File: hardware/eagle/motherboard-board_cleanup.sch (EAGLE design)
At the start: 43 parts, among them U1 DG412DJZ, Y1 16MHz

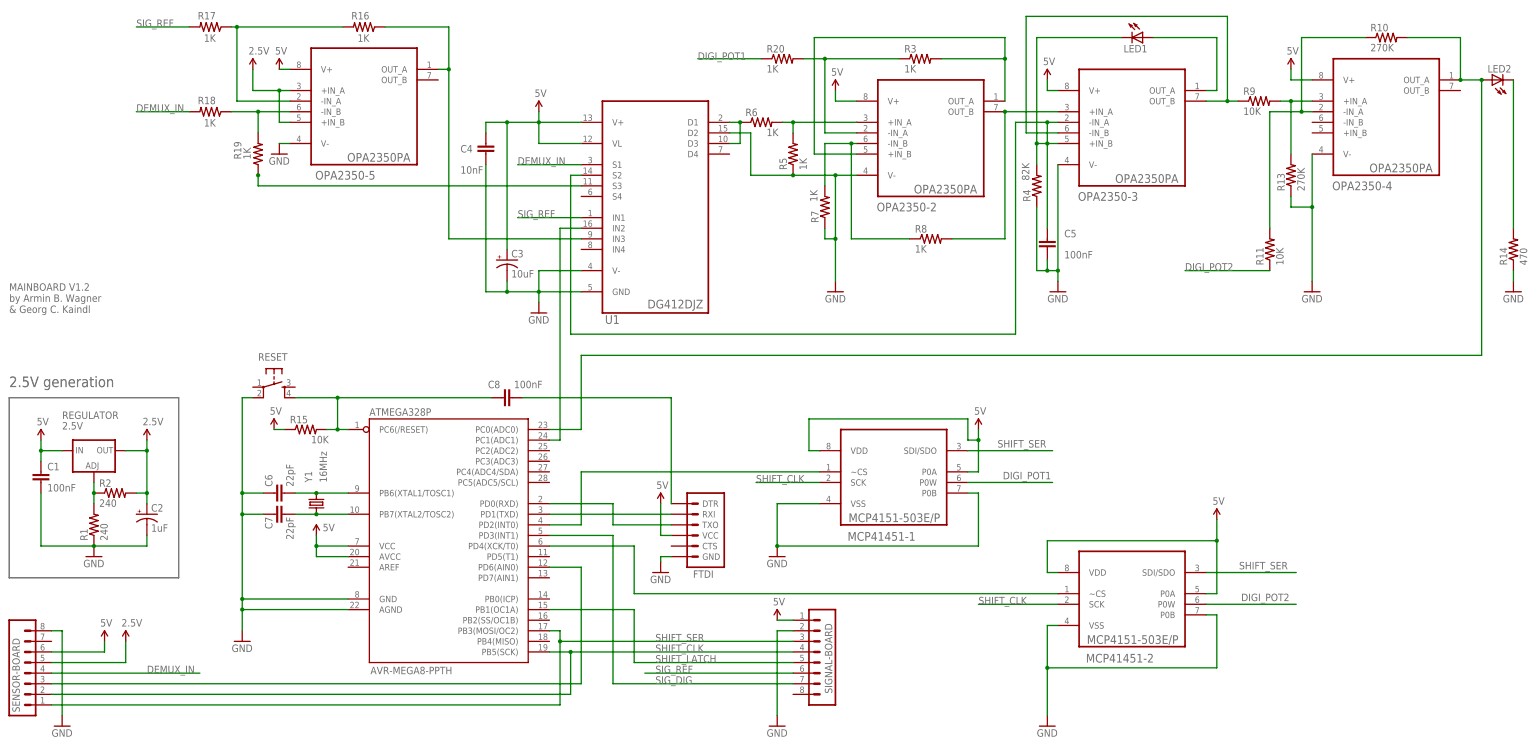
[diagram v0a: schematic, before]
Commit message: The motherboard's schematic was missing a connection (OUT_B to R19 and the switch's S3). We fixed this using a short wire, but forgot to update the eagle files. Many thanks to Mike Farr for pointing out the mistake!
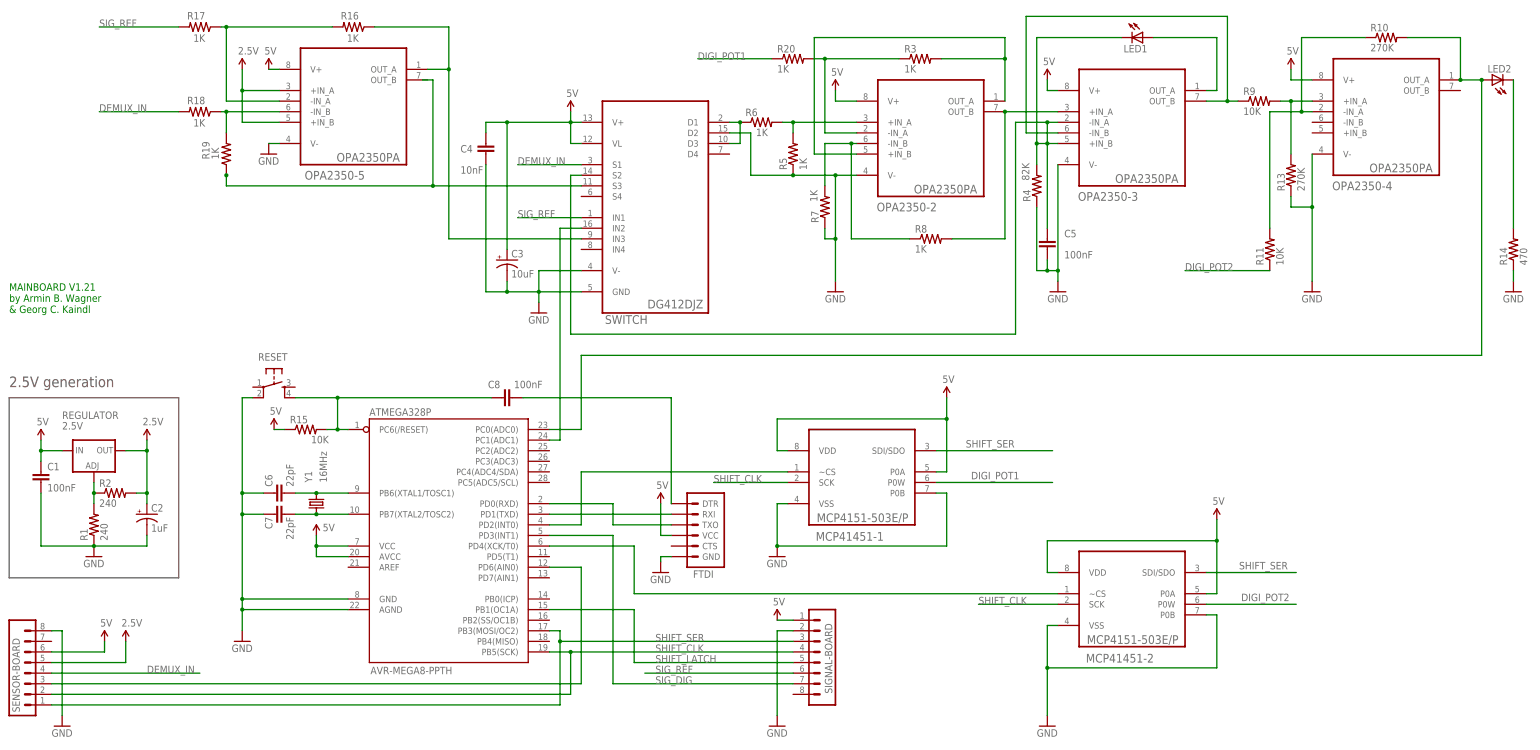
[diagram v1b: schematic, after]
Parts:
- renumbered U1 to SWITCH
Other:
- note added: "MAINBOARD V1.21 by Armin B. Wagner & Georg C. Kaindl"
- note removed: "MAINBOARD V1.2 by Armin B. Wagner & Georg C. Kaindl"
- moved on the sheet: MCP41451-1, OPA2350-5, R16, R17, R18, R19, R20
